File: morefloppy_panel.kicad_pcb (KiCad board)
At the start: 2 copper layers, 71.1 x 45.7 mm, 10 parts, among them J1 PCFloppyHeader, J2 PCFloppyHeader, J3 PCFloppyHeader, J4 PCFloppyHeader, M0 SW_SPDT, M1 SW_SPDT

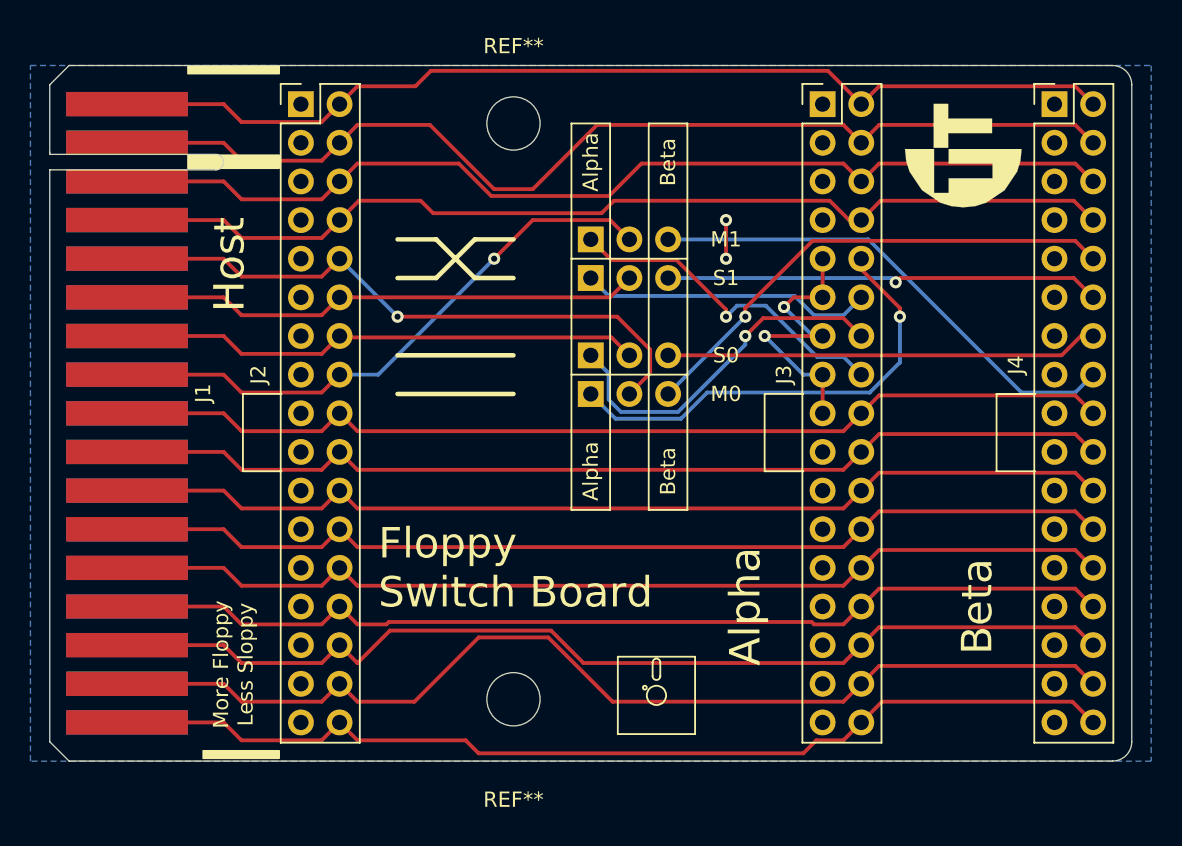
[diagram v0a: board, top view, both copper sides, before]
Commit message: fix silk screen error and generate gerbers
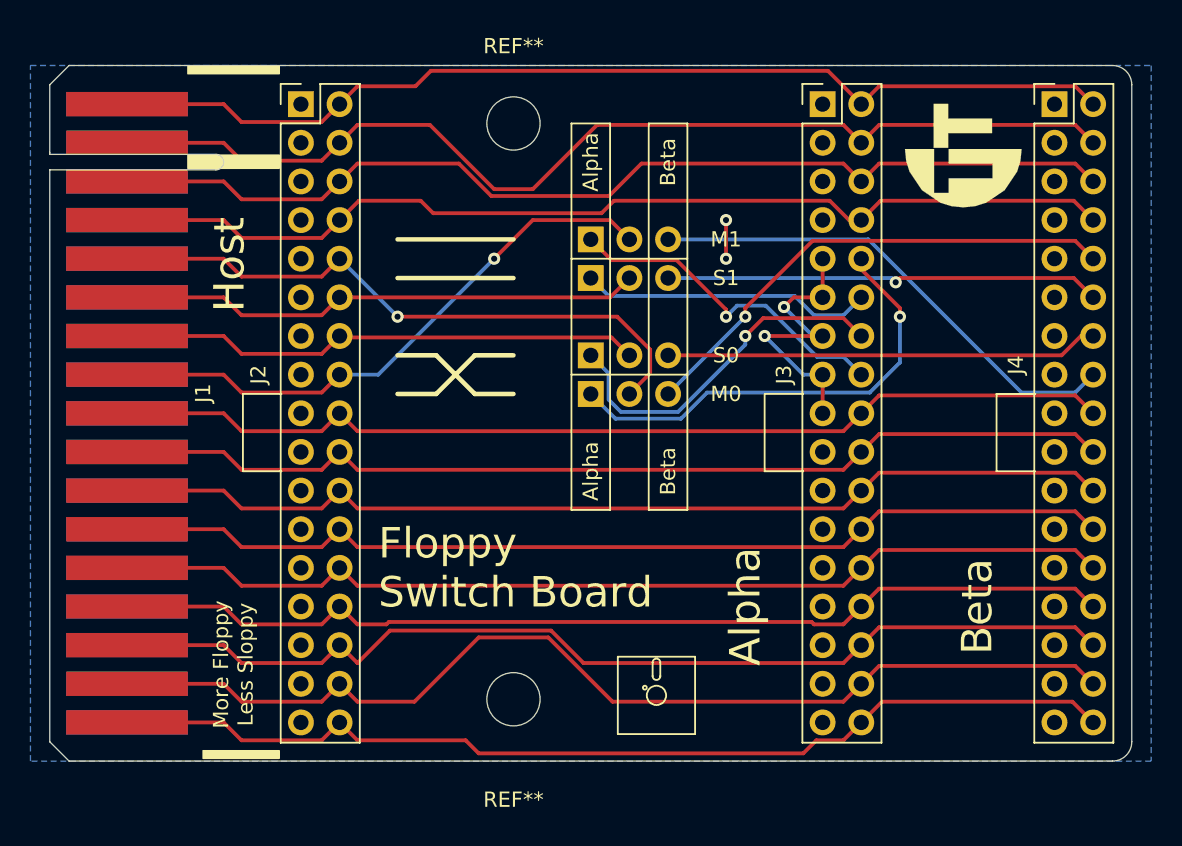
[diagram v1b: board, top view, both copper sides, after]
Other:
- outline, holes or cut-outs redrawn
- net class Default removed
